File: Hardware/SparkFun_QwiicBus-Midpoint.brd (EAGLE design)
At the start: 43.2 x 27.9 mm, 51 parts, among them J1 QWIIC, J2 QWIIC, J3 RJ45, J7 RJ45, U1 PCA9615, U2 3.3V

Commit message: post design review checklist changes
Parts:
- removed J6: (no value), SparkX:1X04_NO_SILK
- added D11: RED, SparkFun-LED:LED-0603
- added J5: (no value), SparkFun-Connectors:1X04_NO_SILK
- added PWR: JUMPER-SMT_2_NC_TRACE_SILK, SparkFun-Jumpers:SMT-JUMPER_2_NC_TRACE_SILK
- added R11: 1k, SparkFun-Resistors:0603
- added U$16, U$18, U$19: (no value), output:#VDDB#0
- added U$17: (no value), output:#VREG#0
- added U$20, U$21: (no value), output:#GND#0
- added U$22: (no value), SparkFun-Aesthetics:QWIIC_4MM
- added U$23: (no value), output:PWR0
- U$11: device output:#5V#0 -> output:#A#B#0
- U$5: device output:#5V#0 -> output:#VDDB#0
- moved A-B 80.1 mm to (22.9, 19.1), flipped to the bottom, turned to 180 degrees
- moved VREG 64.0 mm to (19.1, 10.8), flipped to the bottom, turned to 270 degrees
- moved U$11 19.0 mm to (22.0, 19.1)
- moved U$5 5.59 mm to (7.37, 10.2), flipped to the bottom
- moved U$15 2.54 mm to (20.6, 7.62)
- moved GND\ 2.16 mm to (36.4, 21.7)
- moved VDD_B 2.16 mm to (36.4, 24.2)
- moved JP5 2.16 mm to (36.4, 3.81)
- moved JP6 2.16 mm to (36.4, 6.35)
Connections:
- new net N$13: D11.C, R11.1
- new net N$14: PWR.2, R11.2
- net GND: now also J5.1, PWR.1; no longer J6.1
- net SCL: now also J5.4; no longer J6.4
- net SDA: now also J5.3; no longer J6.3
- net VDD_A: now also D11.A, J5.2; no longer J6.2
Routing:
- net GRN: track 0.00 -> 20.7 mm
- net W_GRN: track 0.00 -> 19.9 mm
- net VDD_A: track 66.6 -> 79.7 mm, vias 2 -> 4
- net VDD_B: track 66.7 -> 73.6 mm, vias 4 -> 5
- net N$8: track 0.00 -> 3.20 mm, vias 0 -> 1
- net N$14: track 0.00 -> 2.04 mm
- net N$2: track 3.65 -> 5.65 mm
- net N$13: track 0.00 -> 1.92 mm
- net N$1: track 9.72 -> 11.1 mm
- net N$5: track 9.80 -> 10.9 mm

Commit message: adding grn pair
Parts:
- removed U$15: (no value), output:QWIICBUS0
- added J6: (no value), SparkFun-Connectors:1X02_NO_SILK
- added U$24, U$25: (no value), output:#GRN#0
- added U$26, U$27: (no value), output:#GRN#W#0
- added U$28, U$30: (no value), output:MIDPOINT0
- added U$29: (no value), output:QWIICBUS0
- LOGO5: value SFE_LOGO_NAME_FLAME.1_INCH -> SFE_LOGO_NAME.1_INCH; device SparkFun-Aesthetics:SFE_LOGO_NAME_FLAME_.1 -> SparkFun-Aesthetics:SFE_LOGO_NAME_.1
- moved U$14 3.53 mm to (6.99, 16.8)
- moved LOGO5 2.54 mm to (12.7, 19.1)
- moved U$23 0.28 mm to (5.21, 8.32)
- moved D11 0.13 mm to (7.49, 2.54)
- moved PWR 0.13 mm to (7.49, 6.35), turned to 270 degrees
- moved R11 0.13 mm to (7.49, 4.45)
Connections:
- removed net GRN: J3.6, J7.6
- removed net W_GRN: J3.3, J7.3
- new net GRN_N: J3.6, J6.2, J7.6
- new net GRN_P: J3.3, J6.1, J7.3
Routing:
- net GRN_N: track 0.00 -> 36.5 mm
- net GRN_P: track 0.00 -> 35.0 mm
- net GRN: track 20.7 -> 0.00 mm
- net W_GRN: track 19.9 -> 0.00 mm
- net VDD_A: track 79.7 -> 77.7 mm
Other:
- board size 43.2 x 27.9 mm -> 45.7 x 27.9 mm

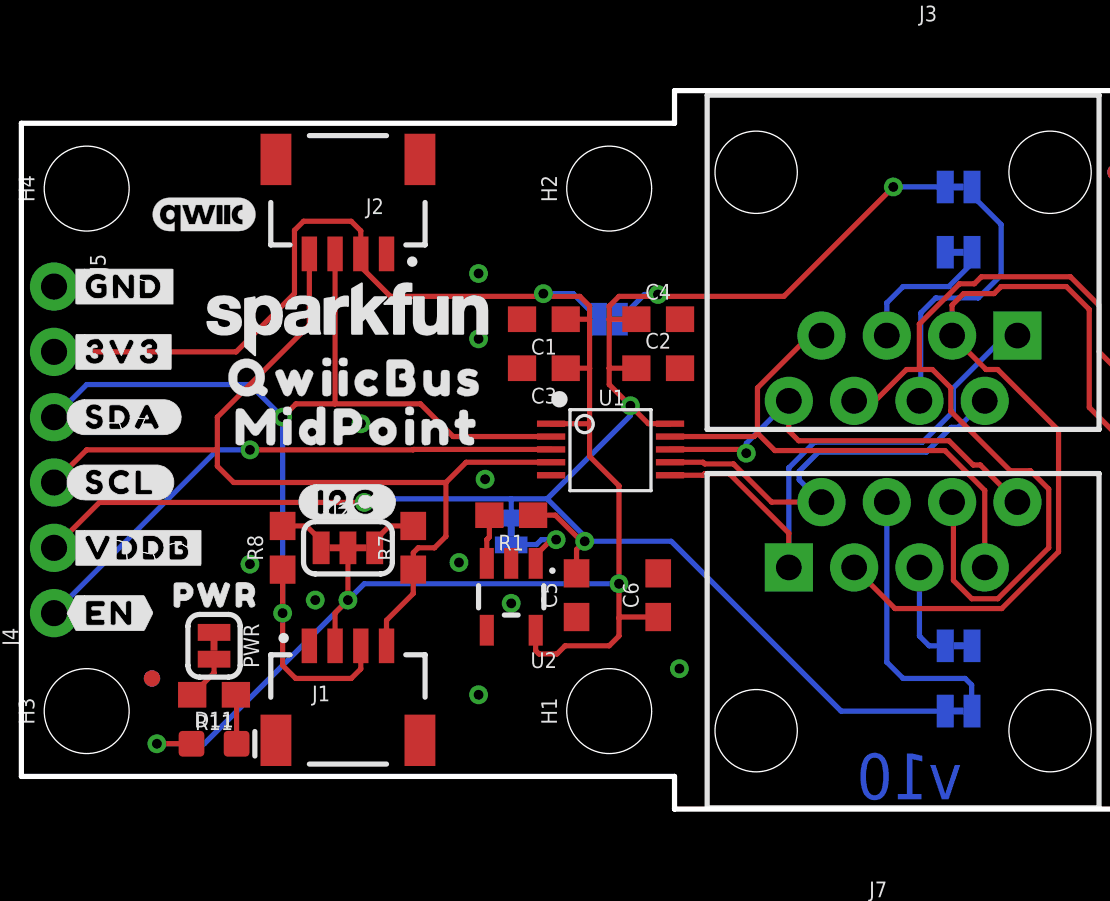
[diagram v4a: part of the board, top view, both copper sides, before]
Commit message: adding qwiicBus silk
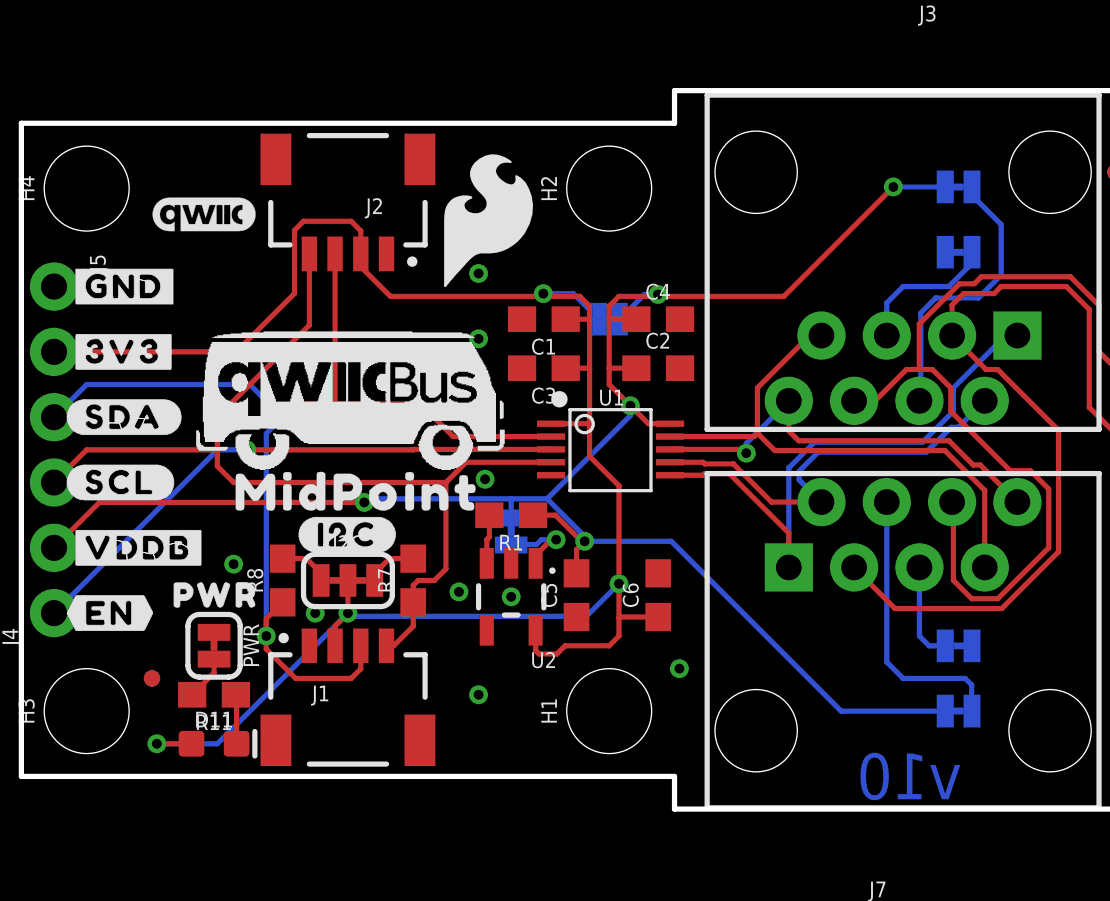
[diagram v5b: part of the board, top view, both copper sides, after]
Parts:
- removed LOGO2: SFE_LOGO_NAME_FLAME.1_INCH, SparkFun-Aesthetics:SFE_LOGO_NAME_FLAME_.1
- removed LOGO5: SFE_LOGO_NAME.1_INCH, SparkFun-Aesthetics:SFE_LOGO_NAME_.1
- removed U$14: (no value), output:QWIICBUS0
- added LOGO3: SFE_LOGO_FLAME.2_INCH, SparkFun-Aesthetics:SFE_LOGO_FLAME_.2
- added LOGO4: SFE_LOGO_NAME_FLAME.1_INCH, SparkFun-Aesthetics:SFE_LOGO_NAME_FLAME_.1
- added U$15: (no value), QwiicBus#working#Logo#jpg (2):QWIICBUS#WORKING#LOGO#JPG
- U$29: device output:QWIICBUS0 -> QwiicBus#working#Logo#jpg (2):QWIICBUS#WORKING#LOGO#JPG
- moved U$29 5.59 mm to (13.2, 16.3), flipped to the top
- moved U$28 2.54 mm to (7.24, 12.3)
- moved U$13 1.27 mm to (10.8, 10.7)
- moved I2C 1.27 mm to (12.7, 8.89)
- moved R7 1.27 mm to (15.2, 8.89)
- moved R8 1.27 mm to (10.2, 8.89)
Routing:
- net VDD_A: track 77.7 -> 76.6 mm

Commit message: pushing mid checklist changes
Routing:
- net GRN_P: track 35.1 -> 33.0 mm
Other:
- outline, holes or cut-outs redrawn
- board text added: "v11"
- board text removed: "v10"
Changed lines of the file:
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@@
 <plain>
 <text x="23.241" y="-14.478" size="1.778" layer="51" font="vector" ratio="10" align="center">Andy England</text>
-<wire x1="45.72" y1="0" x2="25.4" y2="0" width="0.2032" layer="20"/>
-<wire x1="25.4" y1="0" x2="25.4" y2="1.27" width="0.2032" layer="20"/>
+<wire x1="45.72" y1="0" x2="26.67" y2="0" width="0.2032" layer="20"/>
+<wire x1="26.67" y1="0" x2="25.4" y2="1.27" width="0.2032" layer="20"/>
 <wire x1="25.4" y1="1.27" x2="0" y2="1.27" width="0.2032" layer="20"/>
 <wire x1="0" y1="1.27" x2="0" y2="26.67" width="0.2032" layer="20"/>
 <wire x1="0" y1="26.67" x2="25.4" y2="26.67" width="0.2032" layer="20"/>
-<wire x1="25.4" y1="26.67" x2="25.4" y2="27.94" width="0.2032" layer="20"/>
-<wire x1="25.4" y1="27.94" x2="45.72" y2="27.94" width="0.2032" layer="20"/>
+<wire x1="25.4" y1="26.67" x2="26.67" y2="27.94" width="0.2032" layer="20"/>
+<wire x1="26.67" y1="27.94" x2="45.72" y2="27.94" width="0.2032" layer="20"/>
 <wire x1="45.72" y1="27.94" x2="45.72" y2="0" width="0.2032" layer="20"/>
-<text x="36.576" y="0.381" size="1.778" layer="16" font="vector" ratio="15" rot="SMR0">v10</text>
+<text x="36.576" y="0.381" size="1.778" layer="16" font="vector" ratio="15" rot="SMR0">v11</text>
 <dimension x1="0" y1="26.67" x2="45.72" y2="26.67" x3="22.86" y3="36.83" textsize="1.778" layer="47" unit="inch"/>
 <dimension x1="0" y1="1.27" x2="0" y2="26.67" x3="-6.35" y3="13.97" textsize="1.778" layer="47" unit="inch"/>
@@
 <polygon width="0.254" layer="1" isolate="0.3048">
 <vertex x="45.72" y="0"/>
-<vertex x="25.4" y="0"/>
+<vertex x="26.67" y="0"/>
 <vertex x="25.4" y="1.27"/>
 <vertex x="0" y="1.27"/>
 <vertex x="0" y="26.67"/>
 <vertex x="25.4" y="26.67"/>
-<vertex x="25.4" y="27.94"/>
+<vertex x="26.67" y="27.94"/>
 <vertex x="45.72" y="27.94"/>
 </polygon>
 <polygon width="0.254" layer="16" isolate="0.3048">
 <vertex x="45.72" y="0"/>
-<vertex x="25.4" y="0"/>
+<vertex x="26.67" y="0"/>
 <vertex x="25.4" y="1.27"/>
 <vertex x="0" y="1.27"/>
 <vertex x="0" y="26.67"/>
 <vertex x="25.4" y="26.67"/>
-<vertex x="25.4" y="27.94"/>
+<vertex x="26.67" y="27.94"/>
 <vertex x="45.72" y="27.94"/>
 </polygon>
@@
 <polygon width="0.254" layer="16" isolate="0.3048">
 <vertex x="45.72" y="0"/>
-<vertex x="25.4" y="0"/>
+<vertex x="26.67" y="0"/>
 <vertex x="25.4" y="1.27"/>
 <vertex x="0" y="1.27"/>
 <vertex x="0" y="26.67"/>
 <vertex x="25.4" y="26.67"/>
-<vertex x="25.4" y="27.94"/>
+<vertex x="26.67" y="27.94"/>
 <vertex x="45.72" y="27.94"/>
 </polygon>
@@
 <wire x1="32.385" y1="9.3882875" x2="33.9754875" y2="7.7978" width="0.2032" layer="1"/>
 <wire x1="44.45" y1="12.7" x2="41.529" y2="15.621" width="0.2032" layer="1"/>
-<wire x1="41.529" y1="19.431" x2="40.64" y2="20.32" width="0.2032" layer="1"/>
-<wire x1="40.64" y1="20.32" x2="38.1" y2="20.32" width="0.2032" layer="1"/>
-<wire x1="36.195" y1="19.600403125" x2="36.195" y2="18.415" width="0.2032" layer="1"/>
-<wire x1="36.640278125" y1="20.04568125" x2="36.195" y2="19.600403125" width="0.2032" layer="1"/>
-<wire x1="37.82568125" y1="20.04568125" x2="36.640278125" y2="20.04568125" width="0.2032" layer="1"/>
-<wire x1="38.1" y1="20.32" x2="37.82568125" y2="20.04568125" width="0.2032" layer="1"/>
-<wire x1="41.529" y1="15.621" x2="41.529" y2="19.431" width="0.2032" layer="1"/>
+<wire x1="41.529" y1="18.034" x2="39.878" y2="19.685" width="0.2032" layer="1"/>
+<wire x1="39.878" y1="19.685" x2="37.422596875" y2="19.685" width="0.2032" layer="1"/>
+<wire x1="36.195" y1="18.457403125" x2="36.195" y2="18.415" width="0.2032" layer="1"/>
+<wire x1="37.422596875" y1="19.685" x2="36.195" y2="18.457403125" width="0.2032" layer="1"/>
+<wire x1="41.529" y1="15.621" x2="41.529" y2="18.034" width="0.2032" layer="1"/>
 <wire x1="32.385" y1="9.398" x2="32.385" y2="9.3882875" width="0.2032" layer="1"/>
 </signal>
@@
 <wire x1="37.9700125" y1="8.1788" x2="39.9542" y2="10.1629875" width="0.2032" layer="1"/>
 <wire x1="39.9542" y1="10.1629875" x2="39.9542" y2="12.4430125" width="0.2032" layer="1"/>
-<wire x1="44.45" y1="15.24" x2="41.91" y2="17.78" width="0.2032" layer="1"/>
+<wire x1="44.45" y1="15.24" x2="42.545" y2="15.24" width="0.2032" layer="1"/>
+<wire x1="42.545" y1="15.24" x2="41.91" y2="15.875" width="0.2032" layer="1"/>
 <wire x1="32.83921875" y1="15.875" x2="32.385" y2="15.875" width="0.2032" layer="1"/>
-<wire x1="36.482459375" y1="20.42668125" x2="34.9194875" y2="18.863709375" width="0.2032" layer="1"/>
-<wire x1="37.0594" y1="20.42668125" x2="36.482459375" y2="20.42668125" width="0.2032" layer="1"/>
-<wire x1="37.33371875" y1="20.701" x2="37.0594" y2="20.42668125" width="0.2032" layer="1"/>
-<wire x1="41.91" y1="17.78" x2="41.91" y2="19.588825" width="0.2032" layer="1"/>
-<wire x1="41.91" y1="19.588825" x2="40.797825" y2="20.701" width="0.2032" layer="1"/>
-<wire x1="40.797825" y1="20.701" x2="37.33371875" y2="20.701" width="0.2032" layer="1"/>
+<wire x1="36.121778125" y1="20.066" x2="34.9194875" y2="18.863709375" width="0.2032" layer="1"/>
+<wire x1="41.91" y1="15.875" x2="41.91" y2="18.191825" width="0.2032" layer="1"/>
+<wire x1="41.91" y1="18.191825" x2="40.035825" y2="20.066" width="0.2032" layer="1"/>
+<wire x1="40.035825" y1="20.066" x2="36.121778125" y2="20.066" width="0.2032" layer="1"/>
 <wire x1="34.9194875" y1="17.0997125" x2="34.925" y2="17.0942" width="0.2032" layer="1"/>
 <wire x1="34.9194875" y1="18.863709375" x2="34.9194875" y2="17.0997125" width="0.2032" layer="1"/>

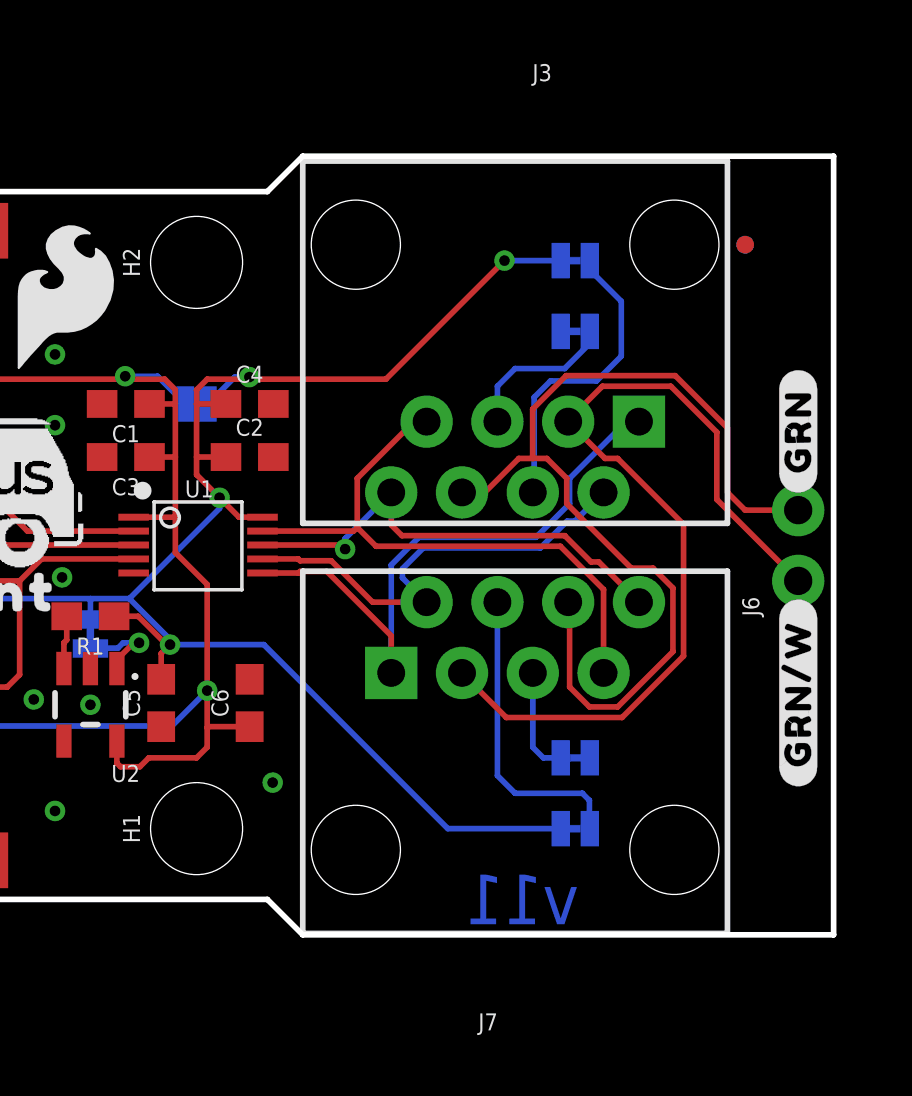
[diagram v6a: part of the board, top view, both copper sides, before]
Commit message: Thickening VDDB
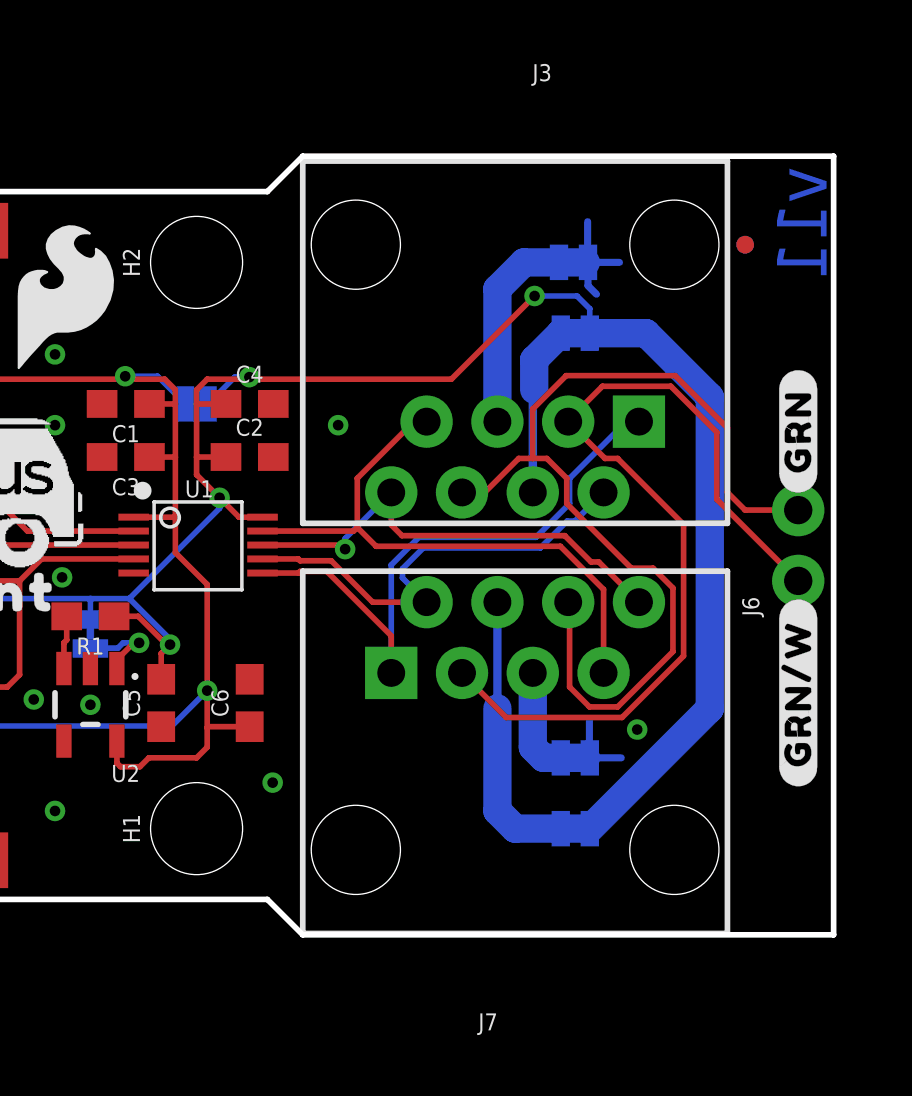
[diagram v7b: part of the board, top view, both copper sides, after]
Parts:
- moved VDD_B 2.60 mm to (36.4, 21.6), turned to 0 degrees
- moved U$21 2.54 mm to (35.6, 24.1)
- moved U$18 2.54 mm to (35.7, 21.7)
- moved GND\ 2.48 mm to (36.4, 24.1), turned to 0 degrees
- turned JP5 to 0 degrees
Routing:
- net VDD_B: track 73.6 -> 81.0 mm
- net GND: track 0.00 -> 6.33 mm, vias 10 -> 12
- net N$1: track 11.1 -> 7.03 mm
- net N$2: track 5.65 -> 8.33 mm
- net N$6: track 3.83 -> 4.73 mm
